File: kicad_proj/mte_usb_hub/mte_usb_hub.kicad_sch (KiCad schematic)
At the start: 4 parts

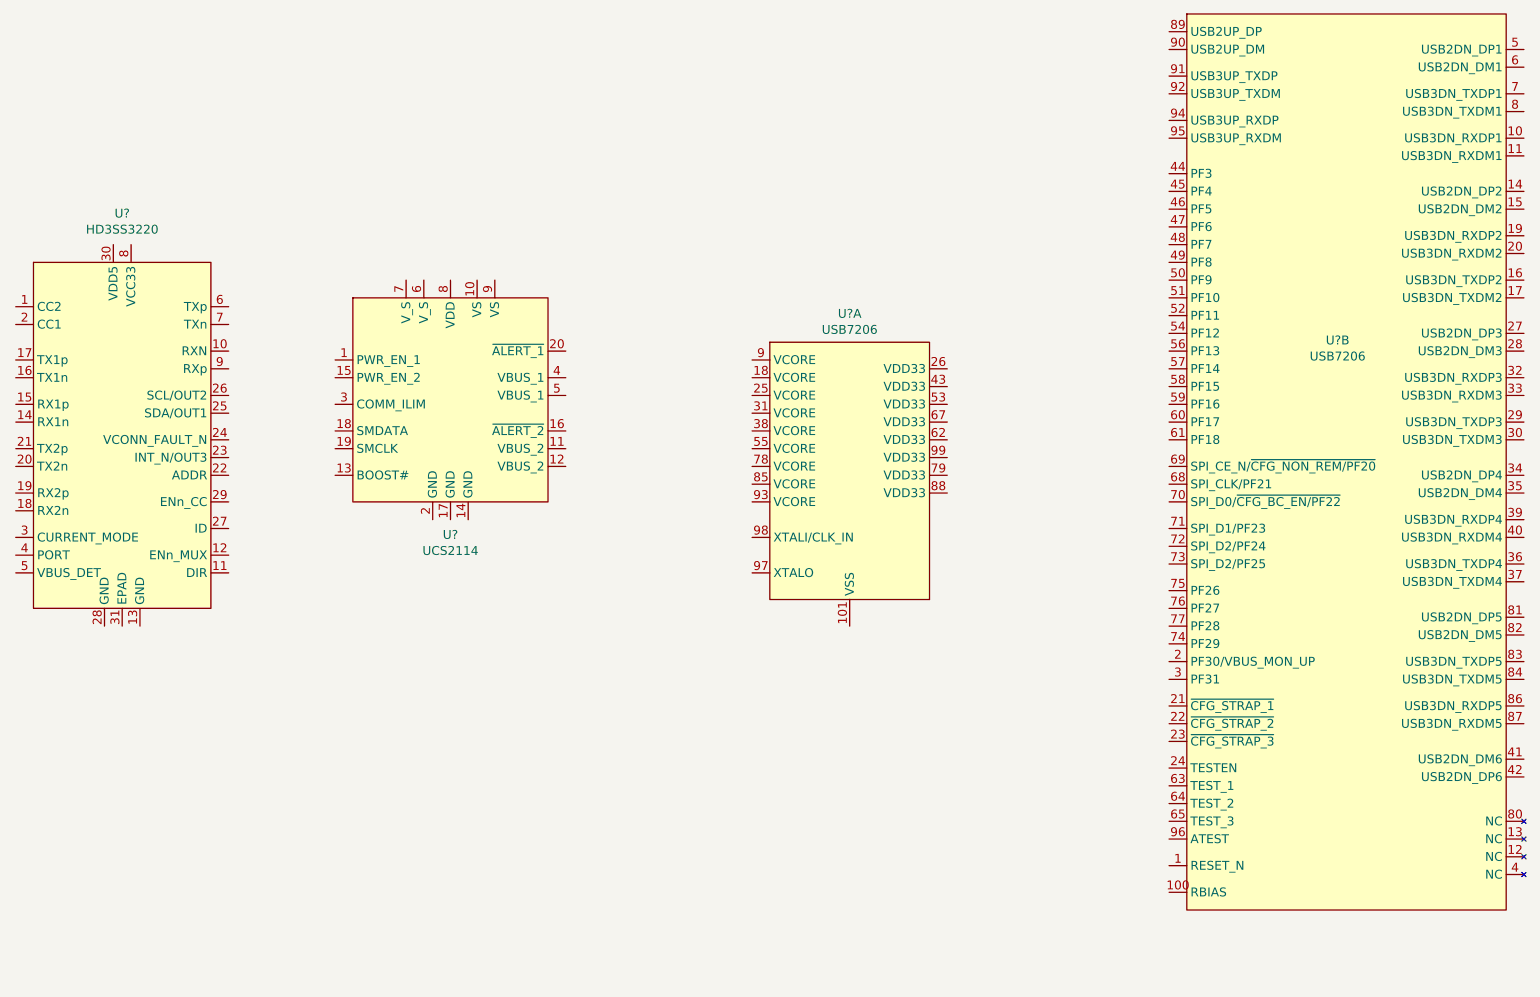
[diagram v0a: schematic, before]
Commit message: Initial setup of USB hub configurations
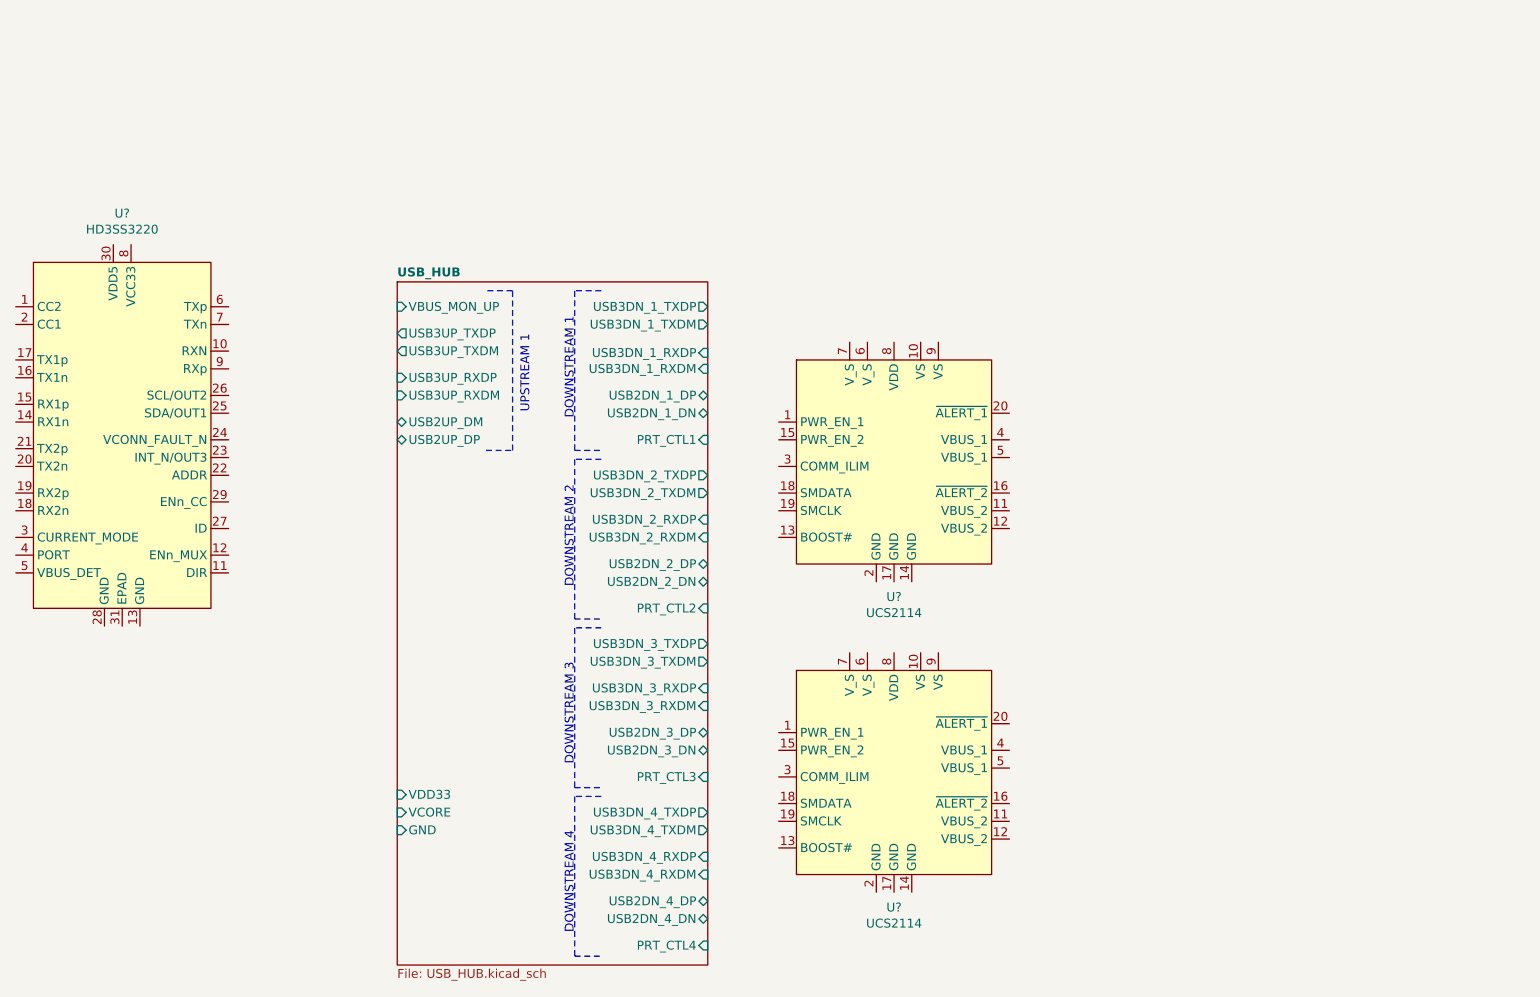
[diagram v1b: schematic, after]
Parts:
- removed U? (x2): USB7206, symbol mte_usb_hub:USB7206
- added U?: UCS2114, symbol mte_usb_hub:UCS2114
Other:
- added sheet USB_HUB (USB_HUB.kicad_sch)
- note added: "DOWNSTREAM 1"
- note added: "DOWNSTREAM 2"
- note added: "DOWNSTREAM 3"
- note added: "DOWNSTREAM 4"
- note added: "UPSTREAM 1"
- moved on the sheet: U?
